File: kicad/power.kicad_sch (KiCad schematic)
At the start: 9 parts, among them J3 Barrel_Jack, U3 TPS62142

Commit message: Finish basic schematic
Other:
- moved on the sheet: D4, J3
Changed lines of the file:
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@@
-	)
-	(junction
-		(at 97.79 97.79)
-		(diameter 0)
-		(color 0 0 0 0)
 	)
 	(junction
@@
 	)
 	(junction
-		(at 88.9 97.79)
+		(at 88.9 95.25)
 		(diameter 0)
 		(color 0 0 0 0)
@@
 	)
 	(junction
+		(at 97.79 95.25)
+		(diameter 0)
+		(color 0 0 0 0)
+	)
+	(junction
+		(at 76.2 95.25)
+		(diameter 0)
+		(color 0 0 0 0)
+	)
+	(junction
 		(at 154.94 105.41)
 		(diameter 0)
@@
 	)
 	(junction
-		(at 76.2 97.79)
-		(diameter 0)
-		(color 0 0 0 0)
-	)
-	(junction
 		(at 121.92 129.54)
 		(diameter 0)
@@
 	(wire
 		(pts
-			(xy 66.04 102.87) (xy 83.82 102.87)
+			(xy 66.04 100.33) (xy 83.82 100.33)
 		)
 		(stroke
@@
 	(wire
 		(pts
-			(xy 88.9 97.79) (xy 88.9 110.49)
+			(xy 88.9 95.25) (xy 88.9 110.49)
 		)
 		(stroke
@@
 	(wire
 		(pts
-			(xy 83.82 102.87) (xy 83.82 129.54)
+			(xy 83.82 100.33) (xy 83.82 129.54)
 		)
 		(stroke
@@
 	(wire
 		(pts
-			(xy 97.79 97.79) (xy 97.79 105.41)
+			(xy 97.79 95.25) (xy 97.79 105.41)
+		)
+		(stroke
+			(width 0)
+			(type default)
+		)
+	)
+	(wire
+		(pts
+			(xy 76.2 95.25) (xy 76.2 83.82)
 		)
 		(stroke
@@
 	(wire
 		(pts
-			(xy 97.79 97.79) (xy 121.92 97.79)
+			(xy 97.79 95.25) (xy 121.92 95.25)
 		)
 		(stroke
@@
 	(wire
 		(pts
-			(xy 66.04 97.79) (xy 67.31 97.79)
+			(xy 66.04 95.25) (xy 67.31 95.25)
 		)
 		(stroke
@@
 	(wire
 		(pts
-			(xy 76.2 97.79) (xy 76.2 83.82)
-		)
-		(stroke
-			(width 0)
-			(type default)
-		)
-	)
-	(wire
-		(pts
-			(xy 76.2 97.79) (xy 88.9 97.79)
+			(xy 76.2 95.25) (xy 88.9 95.25)
 		)
 		(stroke
@@
 	(wire
 		(pts
-			(xy 88.9 97.79) (xy 97.79 97.79)
+			(xy 88.9 95.25) (xy 97.79 95.25)
 		)
 		(stroke
@@
 	(wire
 		(pts
-			(xy 74.93 97.79) (xy 76.2 97.79)
+			(xy 74.93 95.25) (xy 76.2 95.25)
 		)
 		(stroke
@@
 	(wire
 		(pts
+			(xy 121.92 95.25) (xy 121.92 97.79)
+		)
+		(stroke
+			(width 0)
+			(type default)
+		)
+	)
+	(wire
+		(pts
 			(xy 97.79 105.41) (xy 111.76 105.41)
 		)
@@
 	)
 	(label "VIN"
-		(at 82.55 97.79 0)
+		(at 82.55 95.25 0)
 		(effects
 			(font
@@
 	(symbol
 		(lib_id "Connector:Barrel_Jack")
-		(at 58.42 100.33 0)
+		(at 58.42 97.79 0)
 		(unit 1)
 		(exclude_from_sim no)
@@
 		(fields_autoplaced yes)
 		(property "Reference" "J3"
+			(at 58.42 88.9 0)
+			(effects
+				(font
+					(size 1.27 1.27)
+				)
+			)
+		)
+		(property "Value" "Barrel_Jack"
 			(at 58.42 91.44 0)
 			(effects
@@
 			)
 		)
-		(property "Value" "Barrel_Jack"
-			(at 58.42 93.98 0)
-			(effects
-				(font
-					(size 1.27 1.27)
-				)
-			)
-		)
 		(property "Footprint" ""
-			(at 59.69 101.346 0)
+			(at 59.69 98.806 0)
 			(effects
 				(font
@@
 		)
 		(property "Datasheet" "~"
-			(at 59.69 101.346 0)
+			(at 59.69 98.806 0)
 			(effects
 				(font
@@
 		)
 		(property "Description" "DC Barrel Jack"
-			(at 58.42 100.33 0)
+			(at 58.42 97.79 0)
 			(effects
 				(font
@@
 	(symbol
 		(lib_id "Device:D")
-		(at 71.12 97.79 180)
+		(at 71.12 95.25 180)
 		(unit 1)
 		(exclude_from_sim no)
@@
 		(fields_autoplaced yes)
 		(property "Reference" "D4"
+			(at 71.12 88.9 0)
+			(effects
+				(font
+					(size 1.27 1.27)
+				)
+			)
+		)
+		(property "Value" "D"
 			(at 71.12 91.44 0)
 			(effects
@@
 			)
 		)
-		(property "Value" "D"
-			(at 71.12 93.98 0)
-			(effects
-				(font
-					(size 1.27 1.27)
-				)
-			)
-		)
 		(property "Footprint" ""
-			(at 71.12 97.79 0)
+			(at 71.12 95.25 0)
 			(effects
 				(font
@@
 		)
 		(property "Datasheet" "~"
-			(at 71.12 97.79 0)
+			(at 71.12 95.25 0)
 			(effects
 				(font
@@
 		)
 		(property "Description" "Diode"
-			(at 71.12 97.79 0)
+			(at 71.12 95.25 0)
 			(effects
 				(font
@@
 		)
 		(property "Sim.Device" "D"
-			(at 71.12 97.79 0)
+			(at 71.12 95.25 0)
 			(effects
 				(font
@@
 		)
 		(property "Sim.Pins" "1=K 2=A"
-			(at 71.12 97.79 0)
-			(effects
-				(font
+			(at 71.12 95.25 0)
+			(effects
+				(font

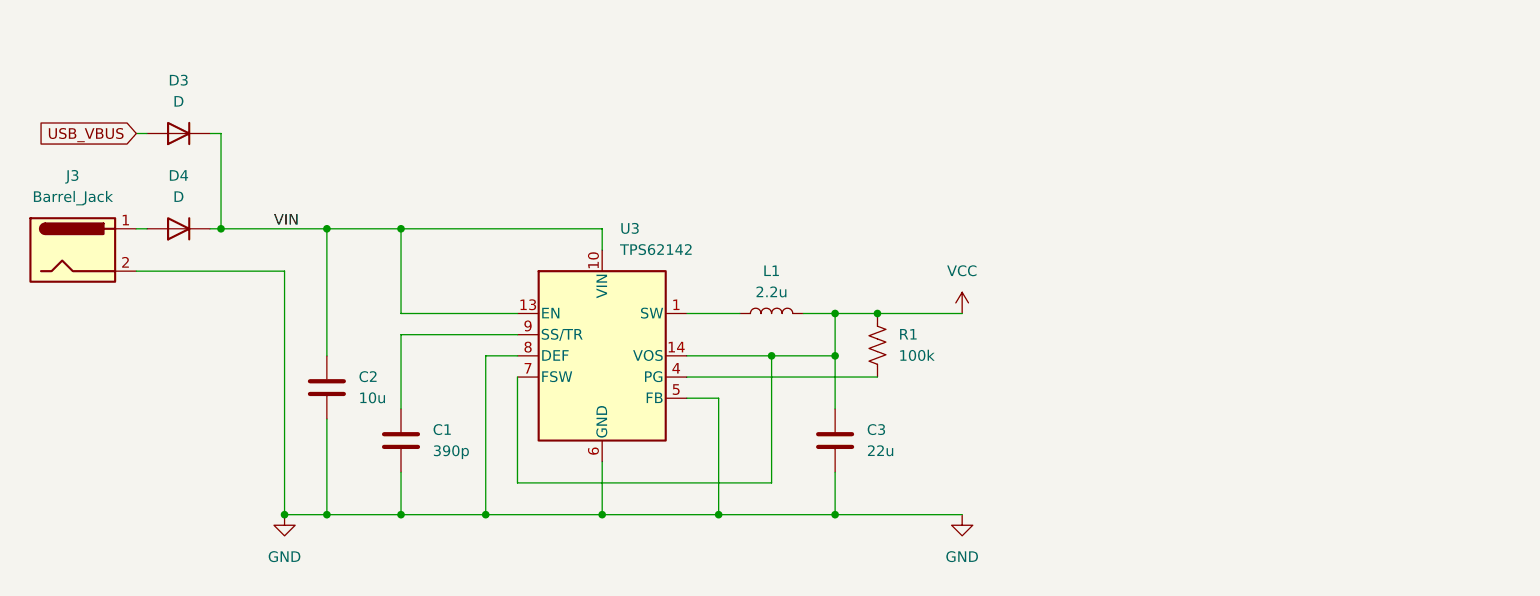
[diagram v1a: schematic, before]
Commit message: Finish schematic and start assigning footprints
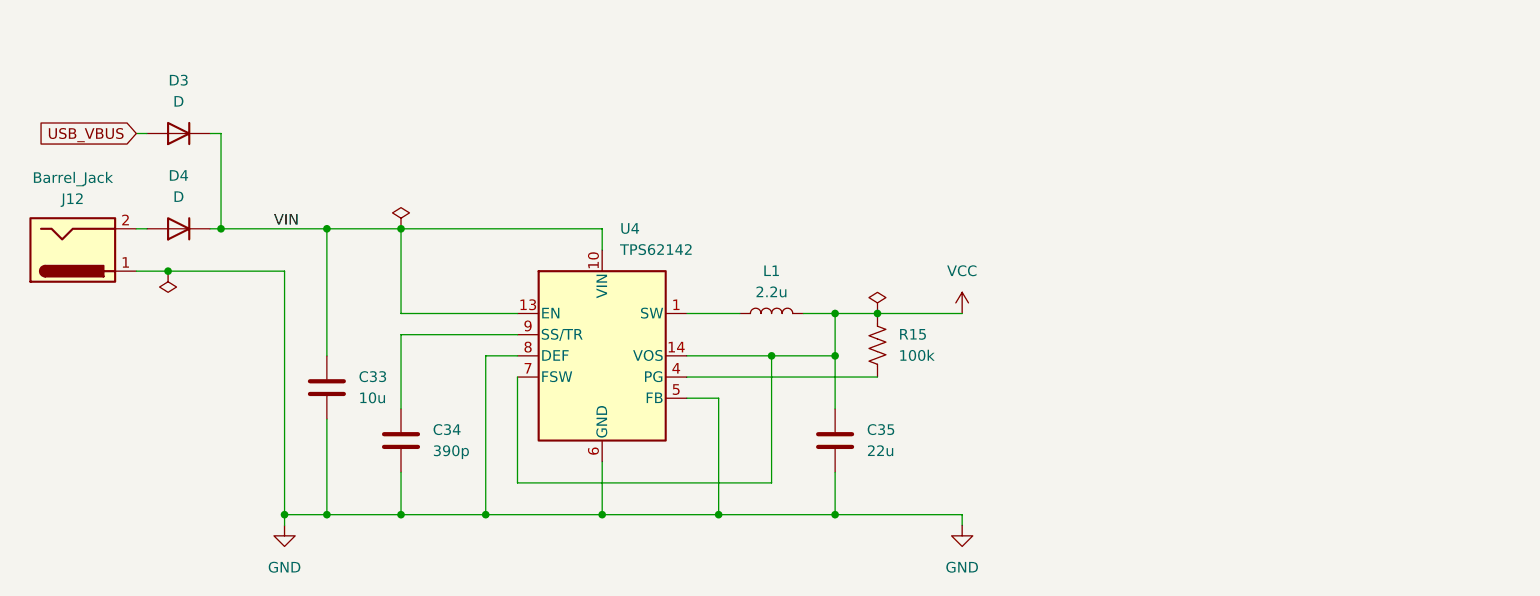
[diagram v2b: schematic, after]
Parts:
- C33: renamed from C2; footprint (none) -> Capacitor_SMD:C_0603_1608Metric
- C34: renamed from C1; footprint (none) -> Capacitor_SMD:C_0603_1608Metric
- C35: renamed from C3; footprint (none) -> Capacitor_SMD:C_0603_1608Metric
- D3, D4: footprint (none) -> Diode_SMD:D_0603_1608Metric
- J12: renamed from J3; footprint (none) -> SameSky:CUI_PJ-002A
- L1: footprint (none) -> Inductor_SMD:L_0603_1608Metric
- R15: renamed from R1; footprint (none) -> Resistor_SMD:R_0603_1608Metric
- renumbered U3 to U4
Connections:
- net GND: now also J12.1; no longer J12.2
- net at D4.2 (A): now also J12.2; no longer J12.1

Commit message: Add more part numbers and VDDA regulator
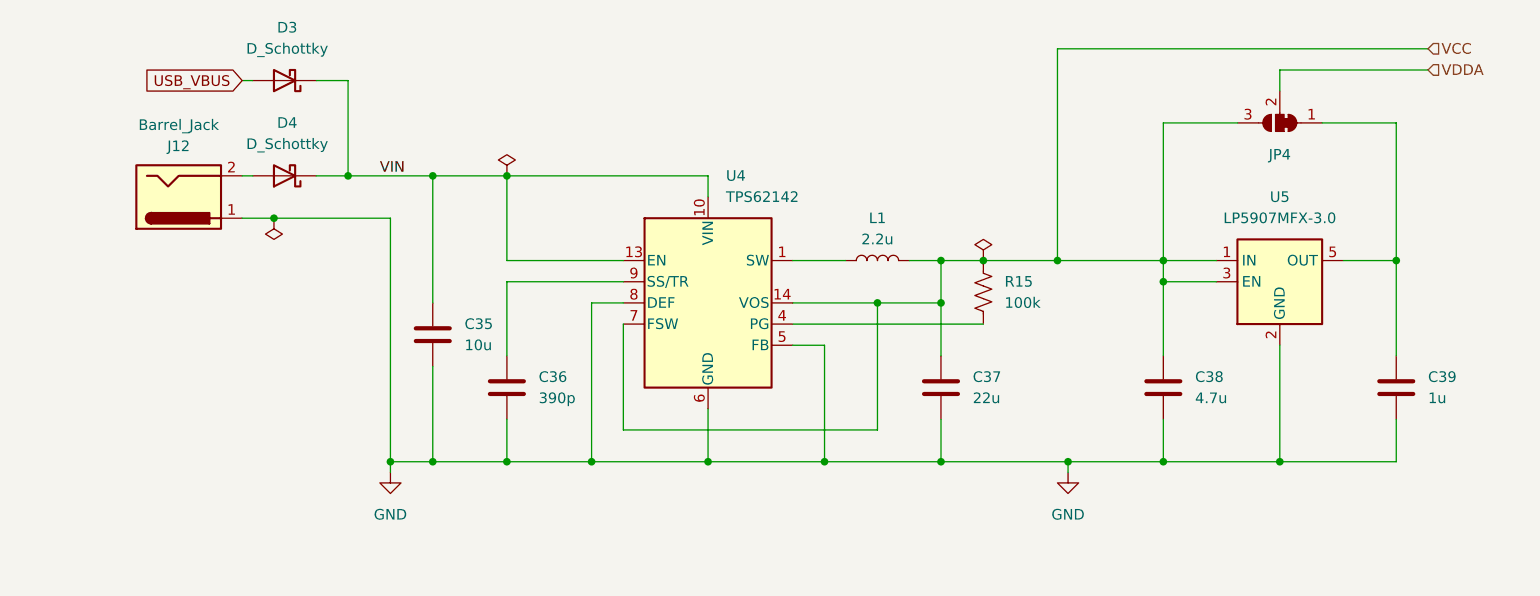
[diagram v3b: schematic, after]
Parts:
- removed D3, D4: D, Diode_SMD:D_0603_1608Metric, symbol Device:D
- added C38: 4.7u, Capacitor_SMD:C_0603_1608Metric, symbol Device:C
- added C39: 1u, Capacitor_SMD:C_0603_1608Metric, symbol Device:C
- added D3, D4: D_Schottky, Diode_SMD:D_SOD-323F, symbol Device:D_Schottky
- added JP4: SolderJumper_3_Bridged12, symbol Jumper:SolderJumper_3_Bridged12
- added U5: LP5907MFX-3.0, Package_TO_SOT_SMD:SOT-23-5, symbol Regulator_Linear:LP5907MFX-3.0
- C35: renamed from C33; Part (none) -> LMK107BBJ106KALT
- C36: renamed from C34; Part (none) -> C0603C391J5GAC
- C37: renamed from C35; Part (none) -> KAM21AT70J226KU
- L1: footprint Inductor_SMD:L_0603_1608Metric -> Inductor_SMD:L_Vishay_IHLP-1212; Part (none) -> IHLP1212BZEV2R2M11
- R15: Part (none) -> Generic
- U4: Part (none) -> TPS62152RGTR
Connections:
- net GND: now also C38.2, C39.2, U5.2 (GND)
- net USB_VBUS: now also D3.2 (A)
- net VCC: now also C38.1, JP4.3 (B), U5.1 (IN), U5.3 (EN)
- net VIN: now also D3.1 (K), D4.1 (K)
- net at J12.2: now also D4.2 (A)
- new net: C39.1, JP4.1 (A), U5.5 (OUT)
- new net VDDA: JP4.2 (C)
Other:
- company: (none) -> ECE 212 Group 2
- title: (none) -> Digital Effect Pedal
- moved on the sheet: C35, C36, C37, J12, L1, R15, U4

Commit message: Add more parts
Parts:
- U4: Part TPS62152RGTR -> TPS62140ARGTR
- U5: Part (none) -> LP5907MFX-3.0
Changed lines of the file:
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@@
+	)
+	(symbol
+		(lib_id "Regulator_Switching:TPS62142")
+		(at 134.62 104.14 0)
+		(unit 1)
+		(exclude_from_sim no)
+		(in_bom yes)
+		(on_board yes)
+		(dnp no)
+		(fields_autoplaced yes)
+		(property "Reference" "U4"
+			(at 136.7633 88.9 0)
+			(effects
+				(font
+					(size 1.27 1.27)
+				)
+				(justify left)
+			)
+		)
+		(property "Value" "TPS62142"
+			(at 136.7633 91.44 0)
+			(effects
+				(font
+					(size 1.27 1.27)
+				)
+				(justify left)
+			)
+		)
+		(property "Footprint" "Package_DFN_QFN:VQFN-16-1EP_3x3mm_P0.5mm_EP1.68x1.68mm_ThermalVias"
+			(at 138.43 115.57 0)
+			(effects
+				(font
+					(size 1.27 1.27)
+				)
+				(justify left)
+				(hide yes)
+			)
+		)
+		(property "Datasheet" "https://www.ti.com/lit/ds/symlink/tps62140.pdf"
+			(at 134.62 104.14 0)
+			(effects
+				(font
+					(size 1.27 1.27)
+				)
+				(hide yes)
+			)
+		)
+		(property "Description" "2A Step-Down Converter with DCS-Control, Fixed 3.3V Output Voltage, 3-17V Input Voltage, QFN-16"
+			(at 134.62 104.14 0)
+			(effects
+				(font
+					(size 1.27 1.27)
+				)
+				(hide yes)
+			)
+		)
+		(property "Part" "TPS62140ARGTR"
+			(at 134.62 104.14 0)
+			(effects
+				(font
+					(size 1.27 1.27)
+				)
+			)
+		)
+		(pin "17"
+		)
+		(pin "3"
+		)
+		(pin "15"
+		)
+		(pin "2"
+		)
+		(pin "13"
+		)
+		(pin "4"
+		)
+		(pin "5"
+		)
+		(pin "6"
+		)
+		(pin "1"
+		)
+		(pin "9"
+		)
+		(pin "8"
+		)
+		(pin "16"
+		)
+		(pin "7"
+		)
+		(pin "10"
+		)
+		(pin "11"
+		)
+		(pin "12"
+		)
+		(pin "14"
+		)
+		(instances
+			(project ""
+				(path "/79bfec23-3e7b-4837-8996-6bbe67be3d6b/50d1ea01-1e05-4a9c-ae07-2b1d5c2735d5"
+					(reference "U4")
+					(unit 1)
+				)
+			)
+		)
 	)
 	(symbol
@@
 			)
 		)
-		(property "Datasheet" "http://www.ti.com/lit/ds/symlink/lp5907.pdf"
+		(property "Datasheet" "https://www.ti.com/lit/ds/symlink/lp5907.pdf?ts=1771413737187"
 			(at 203.2 88.9 0)
 			(effects
@@
 		)
 		(property "Description" "250-mA Ultra-Low-Noise Low-IQ LDO, 3.0V, SOT-23"
+			(at 203.2 101.6 0)
+			(effects
+				(font
+					(size 1.27 1.27)
+				)
+				(hide yes)
+			)
+		)
+		(property "Part" "LP5907MFX-3.0"
 			(at 203.2 101.6 0)
 			(effects
@@
 					(unit 1)
 				)
-			)
-		)
-	)
-	(symbol
-		(lib_id "Regulator_Switching:TPS62142")
-		(at 134.62 104.14 0)
-		(unit 1)
-		(exclude_from_sim no)
-		(in_bom yes)
-		(on_board yes)
-		(dnp no)
-		(fields_autoplaced yes)
-		(property "Reference" "U4"
-			(at 136.7633 88.9 0)
-			(effects
-				(font
-					(size 1.27 1.27)
-				)
-				(justify left)
-			)
-		)
-		(property "Value" "TPS62142"
-			(at 136.7633 91.44 0)
-			(effects
-				(font
-					(size 1.27 1.27)
-				)
-				(justify left)
-			)
-		)
-		(property "Footprint" "Package_DFN_QFN:VQFN-16-1EP_3x3mm_P0.5mm_EP1.68x1.68mm_ThermalVias"
-			(at 138.43 115.57 0)
-			(effects
-				(font
-					(size 1.27 1.27)
-				)
-				(justify left)
-				(hide yes)
-			)
-		)
-		(property "Datasheet" "https://www.ti.com/lit/ds/symlink/tps62140.pdf?ts=1771407972175"
-			(at 134.62 104.14 0)
-			(effects
-				(font
-					(size 1.27 1.27)
-				)
-				(hide yes)
-			)
-		)
-		(property "Description" "2A Step-Down Converter with DCS-Control, Fixed 3.3V Output Voltage, 3-17V Input Voltage, QFN-16"
-			(at 134.62 104.14 0)
-			(effects
-				(font
-					(size 1.27 1.27)
-				)
-				(hide yes)
-			)
-		)
-		(property "Part" "TPS62152RGTR"
-			(at 134.62 104.14 0)
-			(effects
-				(font
-					(size 1.27 1.27)
-				)
-				(hide yes)
-			)
-		)
-		(pin "14"
-		)
-		(pin "16"
-		)
-		(pin "13"
-		)
-		(pin "9"
-		)
-		(pin "8"
-		)
-		(pin "1"
-		)
-		(pin "7"
-		)
-		(pin "6"
-		)
-		(pin "10"
-		)
-		(pin "11"
-		)
-		(pin "15"
-		)
-		(pin "4"
-		)
-		(pin "3"
-		)
-		(pin "17"
-		)
-		(pin "5"
-		)
-		(pin "2"
-		)
-		(pin "12"
-		)
-		(instances
-			(project "power"
-				(path "/04e31104-ef48-40c7-aa44-fb0b2d37d06e"
-					(reference "U?")
-					(unit 1)
-				)
-			)
-			(project "effect-pedal"
-				(path "/79bfec23-3e7b-4837-8996-6bbe67be3d6b/50d1ea01-1e05-4a9c-ae07-2b1d5c2735d5"
-					(reference "U4")
-					(unit 1)
-				)
